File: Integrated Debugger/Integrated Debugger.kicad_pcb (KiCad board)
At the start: 4 copper layers, 36.8 x 16.4 mm, 61 parts, among them J1 B2B GT-B0353FSV06-08B0201, J2 USB_C (PC <-> Host), J3 FPC socket 10P, J4 20021521-00010T1LF, J5 PWR, Q1 NMOS DMN2991UDA-7B, Q2 Generic N-MOSFET, SW1 BOOT, SW2 RESET, SW3 Auxiliary Override, SW4 Target Override, U1 USBULC6-2M6, U2 STM32F103CBUx, U3 TXB0106RGY, U4 TPS7A2633DRVR, U5 TPS22914, U6 TPS22914, Y1 8MHz

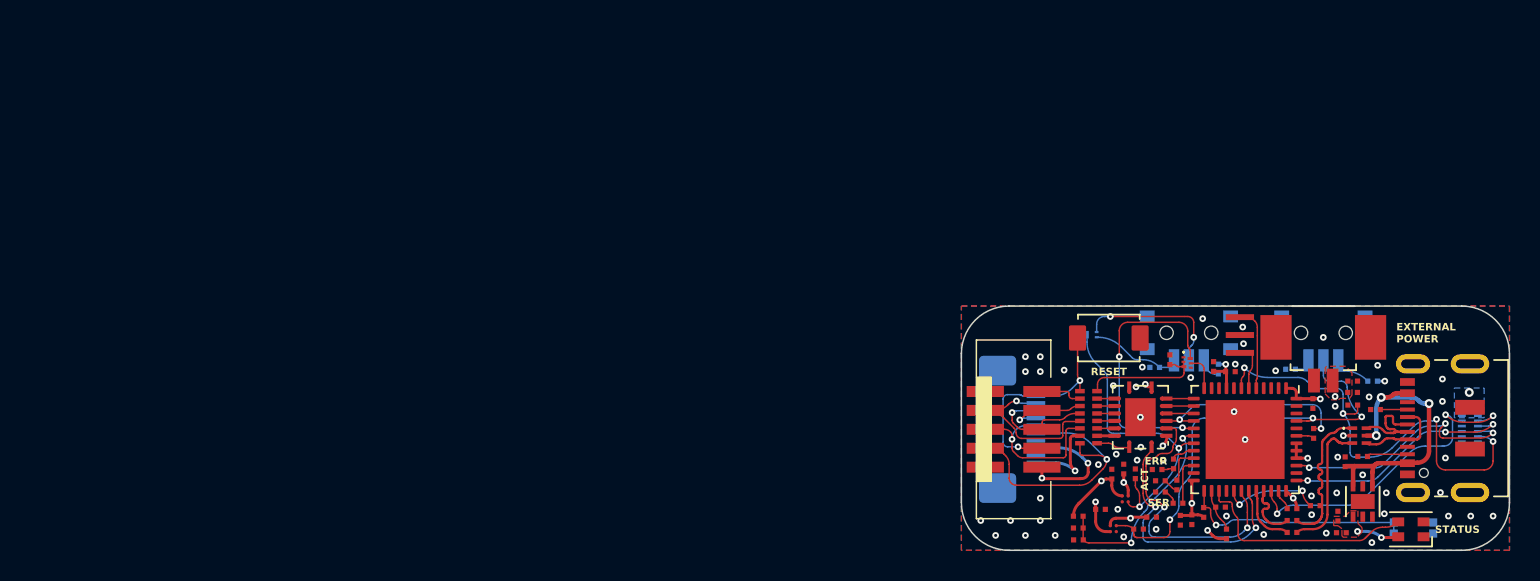
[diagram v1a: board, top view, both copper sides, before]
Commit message: Integrated debugger PCB
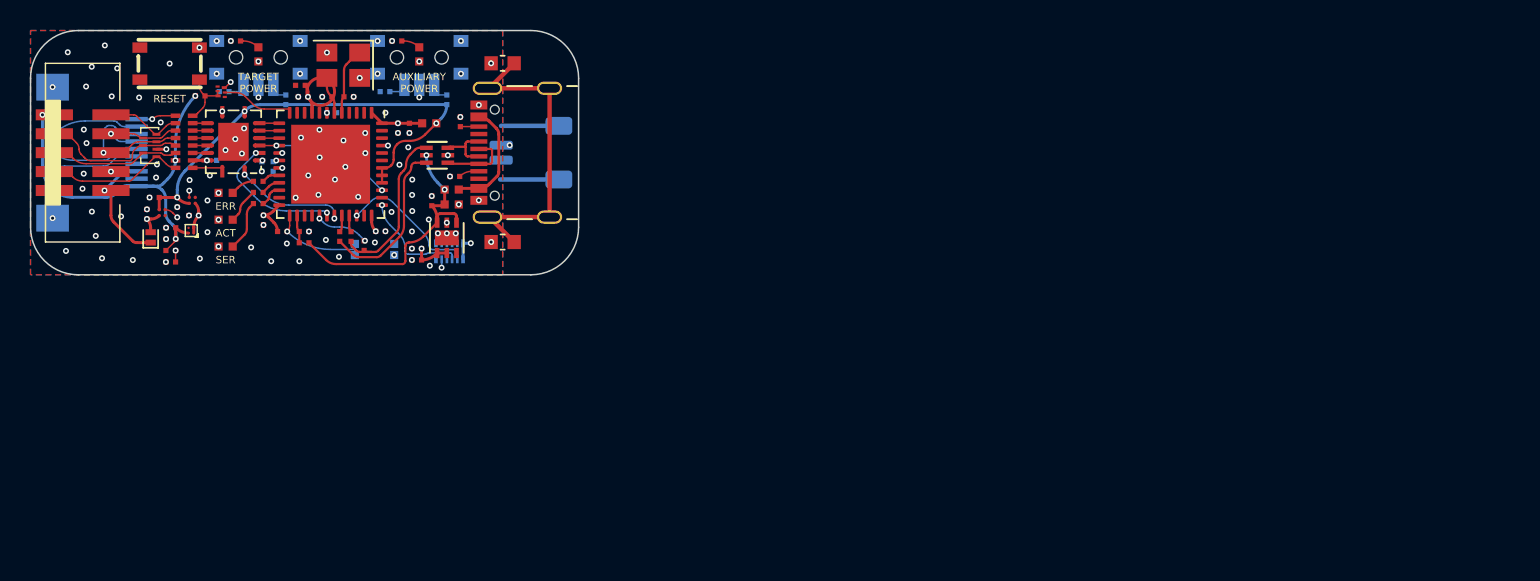
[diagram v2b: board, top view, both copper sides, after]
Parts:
- removed D1: XL-2121RGBC-WS2812B, Picoballoon ICs:WS2812B-2121
- removed Q2: Generic N-MOSFET, Picoballoon ICs:PICOSTAR-3_0.65
- removed R9: 0Ω, Picoballoon Passives:Resistor 0201
- added C18: 100nF, Picoballoon Passives:Capacitor 0201, B.Cu at (93.4, 67.8)
- added C19: 100nF, Picoballoon Passives:Capacitor 0201, B.Cu at (96.7, 68.2)
- added C20: 18pF, Picoballoon Passives:Capacitor 0201, F.Cu at (102.6, 63.5)
- added C21: 18pF, Picoballoon Passives:Capacitor 0201, F.Cu at (101.1, 63.5)
- added C44: 1µF, Picoballoon Passives:Capacitor 0201, F.Cu at (91.0, 70.6)
- added C45: 1µF, Picoballoon Passives:Capacitor 0201, F.Cu at (89.5, 70.3)
- added D12: PUSB3AB6Z, Picoballoon ICs:XSON-7, F.Cu at (89.2, 66.8)
- added D5: ORANGE, Picoballoon Passives:LED 0402, F.Cu at (96.5, 60.7)
- added D6: ORANGE, Picoballoon Passives:LED 0402, F.Cu at (107.3, 60.7)
- added D7: CFSH05-20L TR PBFREE, Picoballoon Passives:Diode SOD-882, F.Cu at (89.3, 73.0)
- added FB1: 1000Ω, Picoballoon Passives:Inductor 0402, F.Cu at (109.5, 69.8)
- added FB4: 1000Ω, Picoballoon Passives:Inductor 0402, F.Cu at (108.0, 65.3)
- added R22: 5.1kΩ, Picoballoon Passives:Resistor 0201, F.Cu at (109.7, 68.9)
- added U4: MAX40200, Picoballoon ICs:WLP-4, F.Cu at (92.0, 72.5)
- C1, C17: moved to B.Cu
- C14: value 1μF -> 4.7μF
- C8: value 100nF -> 4.7nF; footprint Picoballoon Passives:Capacitor 0201 -> Picoballoon Passives:Capacitor 0603
- C9: value 100nF -> 10μF; footprint Picoballoon Passives:Capacitor 0201 -> Picoballoon Passives:Capacitor 0402
- D2: value RED -> ERR; footprint Picoballoon Passives:LED 0201 -> Picoballoon Passives:LED 0402
- D3: value ORANGE -> ACT; footprint Picoballoon Passives:LED 0201 -> Picoballoon Passives:LED 0402
- D4: value YELLOW -> SER; footprint Picoballoon Passives:LED 0201 -> Picoballoon Passives:LED 0402
- J3: footprint Picoballoon Mechanical & Misc:FPC connector FPC-05F-10PH20 -> Picoballoon Mechanical & Misc:FH28-10S-0.5SH(05)
- J5: footprint Picoballoon Mechanical & Misc:MOLEX 532610271 -> Picoballoon Mechanical & Misc:JST-SH-2P; moved to B.Cu
- J6: renamed from J2; value USB_C (PC <-> Host) -> TYPE-C-31-M-12; footprint Picoballoon Mechanical & Misc:USB-C DX07S016JA1R1500 -> Picoballoon Mechanical & Misc:TYPE-C-31-M-12
- Q1: value NMOS DMN2991UDA-7B -> DMN31D5UDA-7B
- R1: value 1.5kΩ -> 560Ω
- R14: value 10kΩ -> 1MΩ; footprint Picoballoon Passives:Resistor 0201 -> Picoballoon Passives:Resistor 0603
- R15: value 10kΩ -> 5.1kΩ
- R2, R3: value 1.5kΩ -> 470Ω
- R7, R8: value 1.5kΩ -> 1kΩ
- SW3: value Auxiliary Override -> AUXILIARY POWER
- SW5: renamed from SW2; footprint Picoballoon Mechanical & Misc:Button GT-TC029B-H025-L1N -> Picoballoon Mechanical & Misc:SMD-4P 4.2x3.2mm
- U5: renamed from U1; value USBULC6-2M6 -> USBLC6-2P6; footprint Picoballoon ICs:UQFN-6 -> Picoballoon ICs:SOT-666-6
- U8: renamed from U5; value TPS22914 -> TPS22916
- U9: renamed from U6; value TPS22914 -> TPS22916
- Y1: footprint Picoballoon Passives:Crystal 3213-3P -> Picoballoon Passives:Crystal 3225
- moved R7 80.6 mm to (95.0, 59.8)
- moved C16 80.1 mm to (90.6, 72.3), turned to 180 degrees
- moved C15 79.9 mm to (90.6, 73.1), turned to 180 degrees
- moved SW1 72.2 mm to (104.3, 73.8)
- moved C1 71.3 mm to (101.4, 64.6), turned to 180 degrees
- moved R8 70.2 mm to (105.8, 59.8)
- moved J1 69.5 mm to (109.3, 73.9), turned to 180 degrees
- moved R13 67.5 mm to (92.6, 63.5), turned to 0 degrees
- moved Q1 67.4 mm to (94.0, 63.2)
- moved U8 67.3 mm to (90.0, 71.3)
- moved C13 67.0 mm to (89.0, 71.4), turned to 90 degrees
- moved J6 67.0 mm to (113.5, 67.3)
- moved R5 67.0 mm to (102.0, 72.9), turned to -90 degrees
- moved R4 66.2 mm to (103.6, 73.5), turned to -90 degrees
- moved R6 66.0 mm to (102.7, 72.9), turned to -90 degrees
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- renumbered U4 to U1
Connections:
- net xTPWR renamed Net-(RN1G-R7.2)
- C10 pad 1: +5V -> VDD_USB
- C11 pad 1: +3.3V -> VDD_3V3
- C12 pad 1: V_TARGET -> Net-(D5-K)
- C13 pad 1: V_AUX -> Net-(D6-K)
- C14 pad 1: +3.3V -> VDD_3V3
- C15 pad 1: V_AUX -> VDD_TG
- C16 pad 1: V_AUX -> VDD_TG
- C2 pad 2: +3.3V -> VDD_GPIO
- C3 pad 2: +3.3V -> VDD_GPIO
- C4 pad 2: +3.3V -> VDD_GPIO
- C5 pad 2: +3.3V -> VDD_GPIO
- C6 pad 2: +3.3V -> VDD_GPIO
- C7 pad 2: +3.3V -> VDD_GPIO
- C8 pad 1: +3.3V -> /SHLD
- C9 pad 1: +3.3V -> VDD_USB
- J1 pad 6: /MCU/TRACESWO -> unconnected-(J1-Pin_6-Pad6)
- J1 pad P1: +3.3V -> VDD_3V3
- J1 pad P1_2: +3.3V -> VDD_3V3
- J3 pad 1: V_TARGET -> VDD_TG
- J3 pad 3: V_AUX -> VDD_AUX
- J4 pad 1: V_TARGET -> VDD_TG
- J4 pad 10: V_AUX -> VDD_AUX
- J5 pad 1: V_AUX -> VDD_TG
- J6 pad A4: +5V -> Net-(FB1-Pad2)
- J6 pad A5: Net-(J2-CC1) -> Net-(J6-CC1)
- J6 pad A9: +5V -> Net-(FB1-Pad2)
- J6 pad B4: +5V -> Net-(FB1-Pad2)
- J6 pad B5: Net-(J2-CC2) -> Net-(J6-CC2)
- J6 pad B9: +5V -> Net-(FB1-Pad2)
- J6 pad S1: GND -> /SHLD
- R10 pad 1: +3.3V -> VDD_GPIO
- R11 pad 1: V_TARGET -> VDD_TG
- R13 pad 1: TARGET -> VDD_TG
- R14 pad 1: /MCU/AUX_EN -> /SHLD
- R15 pad 1: /MCU/TARGET_EN -> Net-(J6-CC2)
- R16 pad 1: +3.3V -> VDD_3V3
- R18 pad 1: +3.3V -> VDD_3V3
- R20 pad 1: +5V -> VDD_USB
- R7 pad 1: Net-(J2-CC1) -> Net-(D5-A)
- R8 pad 1: Net-(J2-CC2) -> Net-(D6-A)
- RN1 pad 7: V_TARGET -> VDD_TG
- SW4 pad 2: Net-(Q2-G) -> /MCU/TG_EN
- SW5 pad 1: GND -> unconnected-(SW5-Pad1)
- SW5 pad 2: /Target/tRST -> GND
- U1 pad 1: +3.3V -> VDD_3V3
- U1 pad 2: unconnected-(U4-NC-Pad2) -> VDD_3V3
- U1 pad 4: +5V -> VDD_USB
- U1 pad 6: +5V -> VDD_USB
- U2 pad 1: +3.3V -> VDD_GPIO
- U2 pad 19: /MCU/TARGET_EN -> /MCU/TG_EN
- U2 pad 24: +3.3V -> VDD_GPIO
- U2 pad 27: /MCU/LEDX -> unconnected-(U2A-PB14-Pad27)
- U2 pad 36: +3.3V -> VDD_GPIO
- U2 pad 39: /MCU/TRACESWO -> /MCU/i.TDO
- U2 pad 40: +3.3V -> VDD_3V3
- U2 pad 41: +3.3V -> VDD_3V3
- U2 pad 42: +3.3V -> VDD_3V3
- U2 pad 43: Net-(U2-PB7) -> unconnected-(U2A-PB7-Pad43)
- U2 pad 48: +3.3V -> VDD_GPIO
- U2 pad 5: Net-(U2-PD0) -> Net-(U2B-PD0)
- U2 pad 6: Net-(U2-PD1) -> Net-(U2B-PD1)
- U2 pad 9: +3.3V -> VDD_GPIO
- U3 pad 2: +3.3V -> VDD_3V3
- U3 pad 8: +3.3V -> VDD_3V3
- U5 pad 1: /USBX.D+ -> /D-
- U5 pad 3: /USBX.D- -> /D+
- U5 pad 4: /D- -> /USBX.D+
- U5 pad 5: +5V -> VDD_USB
- U5 pad 6: /D+ -> /USBX.D-
- U8 pad A1: V_AUX -> Net-(D6-K)
- U8 pad A2: +3.3V -> VDD_3V3
- U9 pad A1: V_TARGET -> Net-(D5-K)
- U9 pad A2: +3.3V -> VDD_3V3
- U9 pad B2: /MCU/TARGET_EN -> /MCU/TG_EN
- Y1 pad 1: Net-(U2-PD1) -> Net-(U2B-PD0)
- Y1 pad 3: Net-(U2-PD0) -> Net-(U2B-PD1)
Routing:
- net V_AUX: track 53.5 -> 0.00 mm, vias 4 -> 0
- net VDD_3V3: track 0.00 -> 52.3 mm, vias 0 -> 6
- net VDD_TG: track 0.00 -> 51.1 mm, vias 0 -> 5
- net +5V: track 40.3 -> 0.00 mm, vias 4 -> 0
- net VDD_GPIO: track 0.00 -> 33.2 mm, vias 0 -> 4
- net Net-(D6-K): track 0.00 -> 28.8 mm, vias 0 -> 2
- net V_TARGET: track 24.3 -> 0.00 mm, vias 3 -> 0
- net /SHLD: track 0.00 -> 22.0 mm
- net +3.3V: track 21.7 -> 0.00 mm, vias 13 -> 0
- net /MCU/TARGET_EN: track 20.6 -> 0.00 mm, vias 2 -> 0
- net VDD_USB: track 0.00 -> 19.0 mm, vias 0 -> 2
- net /MCU/TRACESWO: track 17.1 -> 0.00 mm, vias 3 -> 0
- net /MCU/LEDX: track 16.1 -> 0.00 mm
- net /MCU/~{RST}: track 30.6 -> 15.2 mm, vias 4 -> 2
- net Net-(D5-K): track 0.00 -> 14.5 mm, vias 0 -> 2
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- added copper zone on In4.Cu, net GND
- removed copper zone on B.Cu, net +3.3V
- removed copper zone on F.Cu, net +3.3V
- removed copper zone on In2.Cu, net +3.3V
- removed copper zone on F.Cu, net V_AUX
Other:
- copper layers 4 -> 6
- board text added: "AUXILIARY POWER"
- board text added: "V2.0"
- board text removed: "0"
- board text removed: "0 mm"
- board text removed: "0.0152 mm"
- board text removed: "0.01524 mm"
- board text removed: "0.02"
- board text removed: "0.035 mm"
- board text removed: "0.0900 mm / 0.0900 mm"
- board text removed: "0.0994 mm"
- board text removed: "0.2000 mm"
- board text removed: "0.7 mm"
- board text removed: "1"
- board text removed: "1.0297 mm"
- board text removed: "1.3mm H/HOZ with copper"
- board text removed: "3.8"
- board text removed: "3313 RC57% 4.2mil"
- board text removed: "36.8000 mm x 16.4000 mm"
- board text removed: "4"
- board text removed: "4.4"
- board text removed: "ACT"
- board text removed: "AUX POWER"
- board text removed: "B.Cu"
- board text removed: "B.Mask"
- board text removed: "B.Paste"
- board text removed: "B.Silkscreen"
- board text removed: "BOARD CHARACTERISTICS"
- board text removed: "BOOT"
- board text removed: "Black"
- board text removed: "Board Thickness:"
- board text removed: "Board overall dimensions:"
- board text removed: "Bottom Silk Screen"
- board text removed: "Bottom Solder Mask"
- board text removed: "Bottom Solder Paste"
- board text removed: "Castellated pads:"
- board text removed: "Color"
- board text removed: "Copper Finish:"
- board text removed: "Copper Layer Count:"
- board text removed: "Dielectric 1"
- board text removed: "Dielectric 2"
- board text removed: "Dielectric 3"
- board text removed: "ENIG"
- board text removed: "ERR"
- board text removed: "EXTERNAL POWER"
- board text removed: "Edge card connectors:"
- board text removed: "Epsilon R"
- board text removed: "F.Cu"
- board text removed: "F.Mask"
- board text removed: "F.Paste"
- board text removed: "F.Silkscreen"
- board text removed: "FR4 natural"
- board text removed: "Impedance Control:"
- board text removed: "In1.Cu"
- board text removed: "In2.Cu"
- board text removed: "JLC04101H-3313 JLCPCB stackup"
- board text removed: "Layer Name"
- board text removed: "Loss Tangent"
- board text removed: "Material"
- board text removed: "Min hole diameter:"
- board text removed: "Min track/spacing:"
- board text removed: "No"
- board text removed: "Not specified"
- board text removed: "Plated Board Edge:"
- board text removed: "RESET"
- board text removed: "SER"
- board text removed: "STATUS"
- board text removed: "Thickness (mm)"
- board text removed: "Top Silk Screen"
- board text removed: "Top Solder Mask"
- board text removed: "Top Solder Paste"
- board text removed: "Type"
- board text removed: "V1.1"
- board text removed: "White"
- board text removed: "Yes"
- board text removed: "copper"
- board text removed: "core"
- board text removed: "prepreg"

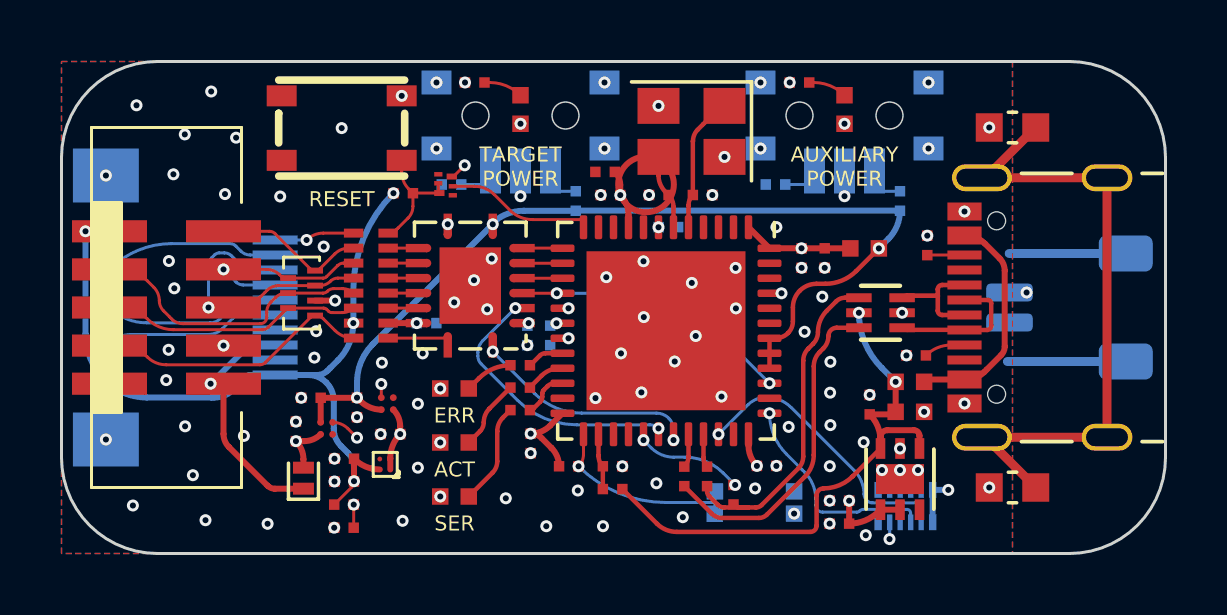
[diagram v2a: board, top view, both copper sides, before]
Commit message: Reannotate schematic, update GND plane
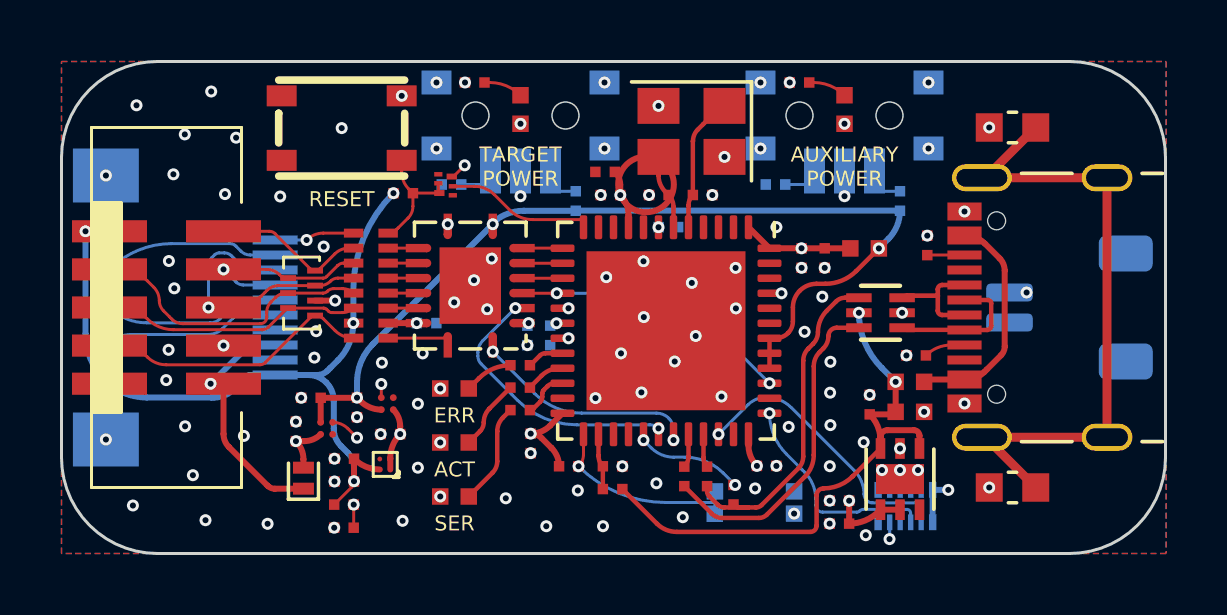
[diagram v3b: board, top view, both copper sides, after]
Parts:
- renumbered C9 to C1, C21 to C10, C17 to C11, C20 to C12, C19 to C13, C18 to C14, C44 to C15, C12 to C16, C10 to C17, C15 to C18, C16 to C19, C8 to C2, C11 to C20, C14 to C21, C45 to C22, C13 to C23, C7 to C3, C6 to C4, C4 to C6, C3 to C7, C2 to C8, C1 to C9, D2 to D1, D3 to D2, D4 to D3, D12 to D4, FB4 to FB2, J6 to J2, R15 to R10, R14 to R11, R10 to R12, R11 to R13, R12 to R14, R13 to R15, R7 to R20, R8 to R21, R20 to R4, R21 to R5, R5 to R6, R6 to R7, R4 to R8, R22 to R9, SW5 to SW2, U5 to U1, U9 to U4, U4 to U5, U1 to U6, U8 to U7
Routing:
- net GND: track 8.55 -> 0.72 mm

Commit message: led+ resistors updated
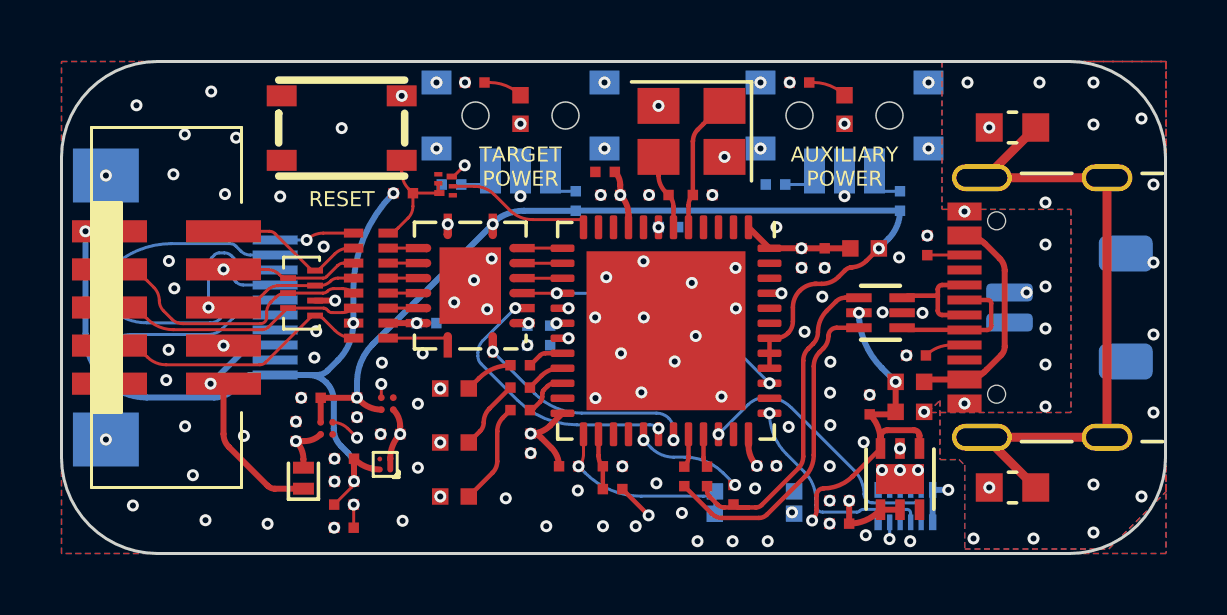
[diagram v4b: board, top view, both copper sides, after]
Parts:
- R1: value 560Ω -> 1kΩ
- R2: value 470Ω -> 4.7kΩ
- R3: value 470Ω -> 220Ω
- moved C20 0.77 mm to (107.1, 73.7)
- moved C21 0.77 mm to (107.1, 74.5)
- renumbered C21 to C20, C20 to C21
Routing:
- net VDD_TG: track 51.1 -> 49.7 mm
- net VDD_GPIO: track 33.2 -> 32.4 mm
- net Net-(R18-Pad2): track 1.52 -> 0.84 mm
- net Net-(R16-Pad2): track 1.53 -> 0.85 mm
- net /SHLD: track 22.0 -> 21.5 mm
- net VDD_USB: track 19.0 -> 18.6 mm, vias 2 -> 4
- net GND: track 0.72 -> 0.67 mm, vias 111 -> 139
- added copper zone on In2.Cu, net GND
- added copper zone on In3.Cu, net GND

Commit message: capacitors updated
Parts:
- C10, C12: value 18pF -> 15pF

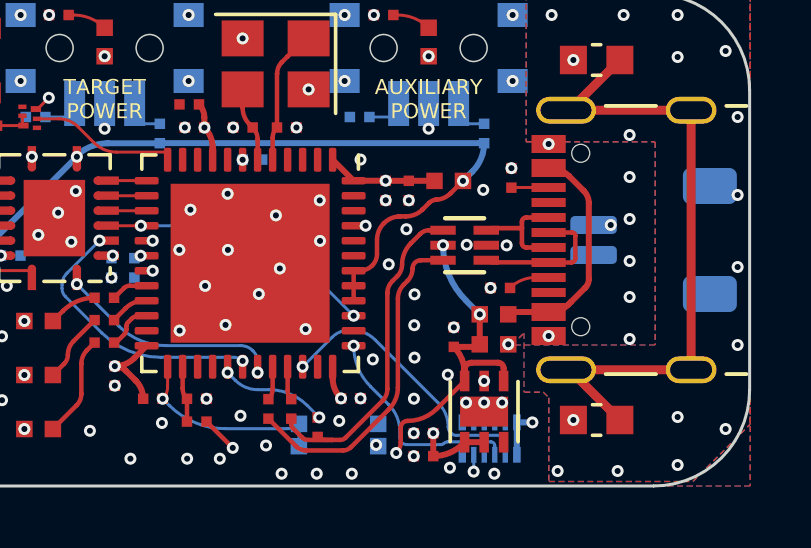
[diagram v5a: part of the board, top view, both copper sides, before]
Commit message: Fix 3D models, add approvals
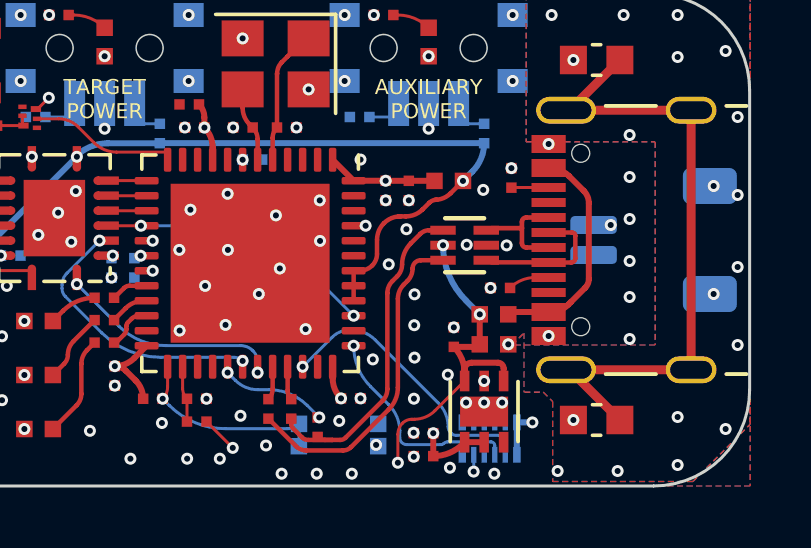
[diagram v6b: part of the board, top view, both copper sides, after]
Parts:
- C18: renamed from C19; value 1μF -> 100nF
- C19: renamed from C18; value 100nF -> 1μF
- renumbered C21 to C20, C20 to C21
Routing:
- net GND: vias 139 -> 141

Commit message: IDBG v2.0 production files
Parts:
- U1: footprint Picoballoon ICs:SOT-666-6 -> Picoballoon ICs:XSON-6
- moved J5 0.62 mm to (114.7, 67.3)
- moved U1 0.40 mm to (108.9, 67.5), turned to -90 degrees
- moved SW3 0.36 mm to (107.3, 61.3), turned to 0 degrees
- moved SW4 0.36 mm to (96.5, 61.3), turned to 0 degrees
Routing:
- net /USBX.D-: track 11.1 -> 12.1 mm
- net /USBX.D+: track 11.3 -> 11.9 mm
